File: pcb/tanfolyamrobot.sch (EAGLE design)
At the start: 78 parts, among them IC1 STM32F10XRXT6, IC2 7805, IC4 FT232RL, IC5 LD117AS33TR, M1 DRV8833, Q2 BSS123, Q3 BSS123, Q4 BSS123, X1 CSTCE08M, X2 PWR, X6 KUSBVX-BS1N

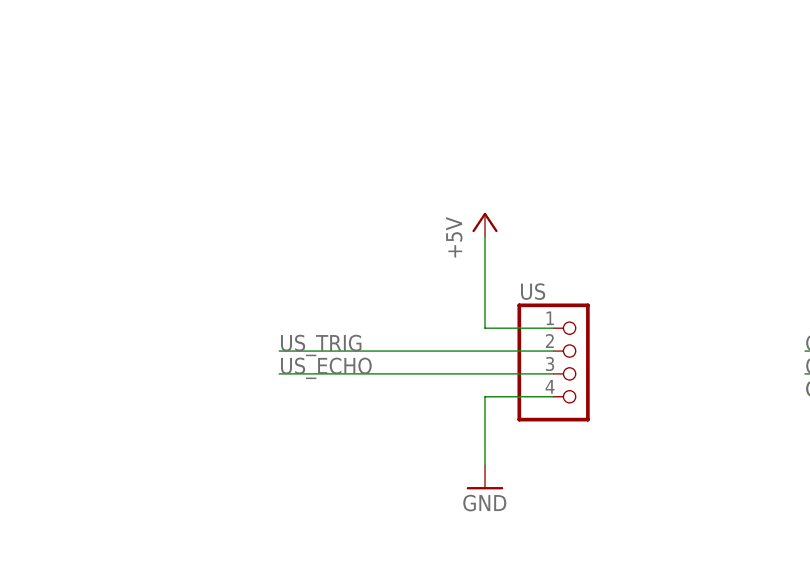
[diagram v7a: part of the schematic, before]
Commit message: added 5V pull-up for ultrasonic trigger (#1)
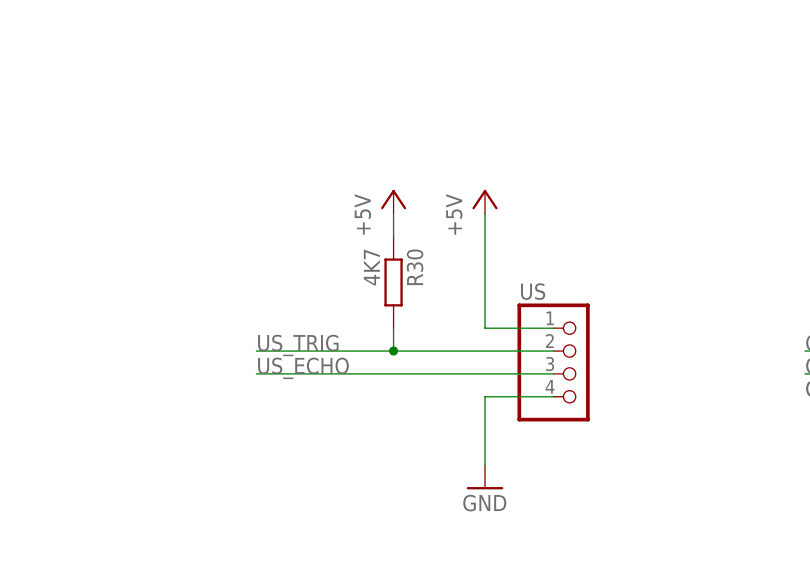
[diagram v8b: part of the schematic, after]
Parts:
- added R30: 4K7, rcl:R-EU_R0603
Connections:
- net +5V: now also R30.1
- net US_TRIG: now also R30.2
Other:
- note added: "Notes: - BUTTON's pin must be pulled up internally - US_TRIG must be operated as open drain output"
- note removed: "Button's pin is pulled up internally"
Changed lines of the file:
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@@
 <part name="SUPPLY3" library="supply2" library_urn="urn:adsk.eagle:library:372" deviceset="+5V/1" device=""/>
 <part name="SUPPLY4" library="supply2" library_urn="urn:adsk.eagle:library:372" deviceset="+5V/1" device=""/>
+<part name="R30" library="rcl" library_urn="urn:adsk.eagle:library:334" deviceset="R-EU_" device="R0603" package3d_urn="urn:adsk.eagle:package:23555/3" value="4K7"/>
+<part name="P+10" library="supply1" library_urn="urn:adsk.eagle:library:371" deviceset="+5V" device=""/>
 </parts>
 <sheets>
@@
 capacitor to connect FTDI output to
 the RESET and/or BOOT0 circuitry</text>
-<text x="297.18" y="210.82" size="1.778" layer="150">Button's pin is
-pulled up internally</text>
+<text x="327.66" y="203.2" size="1.778" layer="150">Notes:
+ - BUTTON's pin must be pulled up internally
+ - US_TRIG must be operated as open drain output</text>
 <text x="429.26" y="83.82" size="1.778" layer="150">Check if backlight resistor is
 required for the used module</text>
@@
 <attribute name="VALUE" x="452.12" y="109.22" size="1.778" layer="96" rot="R90"/>
 </instance>
-<instance part="P+4" gate="1" x="317.5" y="45.72" smashed="yes">
-<attribute name="VALUE" x="314.96" y="40.64" size="1.778" layer="96" rot="R90"/>
+<instance part="P+4" gate="1" x="317.5" y="48.26" smashed="yes">
+<attribute name="VALUE" x="314.96" y="43.18" size="1.778" layer="96" rot="R90"/>
 </instance>
 <instance part="GND13" gate="1" x="317.5" y="15.24" smashed="yes">
@@
 <instance part="SUPPLY4" gate="G$1" x="114.3" y="317.5" smashed="yes">
 <attribute name="VALUE" x="111.125" y="314.325" size="1.778" layer="96" rot="R90"/>
+</instance>
+<instance part="R30" gate="G$1" x="307.34" y="38.1" smashed="yes" rot="R270">
+<attribute name="NAME" x="308.8386" y="41.91" size="1.778" layer="95" rot="R270"/>
+<attribute name="VALUE" x="304.038" y="41.91" size="1.778" layer="96" rot="R270"/>
+</instance>
+<instance part="P+10" gate="1" x="307.34" y="48.26" smashed="yes">
+<attribute name="VALUE" x="304.8" y="43.18" size="1.778" layer="96" rot="R90"/>
 </instance>
 </instances>
@@
 <pinref part="P+4" gate="1" pin="+5V"/>
 <wire x1="325.12" y1="33.02" x2="317.5" y2="33.02" width="0.1524" layer="91"/>
-<wire x1="317.5" y1="33.02" x2="317.5" y2="43.18" width="0.1524" layer="91"/>
+<wire x1="317.5" y1="33.02" x2="317.5" y2="45.72" width="0.1524" layer="91"/>
 <pinref part="US" gate="A" pin="1"/>
 </segment>
@@
 <wire x1="96.52" y1="111.76" x2="91.44" y2="111.76" width="0.1524" layer="91"/>
 </segment>
+<segment>
+<pinref part="R30" gate="G$1" pin="1"/>
+<pinref part="P+10" gate="1" pin="+5V"/>
+<wire x1="307.34" y1="43.18" x2="307.34" y2="45.72" width="0.1524" layer="91"/>
+</segment>
 </net>
 <net name="FTDI_RSTN" class="0">
@@
 <net name="US_TRIG" class="0">
 <segment>
-<wire x1="325.12" y1="30.48" x2="294.64" y2="30.48" width="0.1524" layer="91"/>
-<label x="294.64" y="30.48" size="1.778" layer="95"/>
+<wire x1="325.12" y1="30.48" x2="307.34" y2="30.48" width="0.1524" layer="91"/>
+<label x="292.1" y="30.48" size="1.778" layer="95"/>
 <pinref part="US" gate="A" pin="2"/>
+<pinref part="R30" gate="G$1" pin="2"/>
+<wire x1="307.34" y1="30.48" x2="292.1" y2="30.48" width="0.1524" layer="91"/>
+<wire x1="307.34" y1="33.02" x2="307.34" y2="30.48" width="0.1524" layer="91"/>
+<junction x="307.34" y="30.48"/>
 </segment>
 <segment>
@@
 <net name="US_ECHO" class="0">
 <segment>
-<wire x1="325.12" y1="27.94" x2="294.64" y2="27.94" width="0.1524" layer="91"/>
-<label x="294.64" y="27.94" size="1.778" layer="95"/>
+<wire x1="325.12" y1="27.94" x2="292.1" y2="27.94" width="0.1524" layer="91"/>
+<label x="292.1" y="27.94" size="1.778" layer="95"/>
 <pinref part="US" gate="A" pin="3"/>
 </segment>
